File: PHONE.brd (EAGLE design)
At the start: 127 x 53.3 mm, 105 parts, among them IC1 ATMEGA1284P, IC2 ATMEGA16U2-MU, IC3 LTC4054, IC5 LP2985-33DBVR, J1 Power, J2 Analog, J3 Digital_8_13, J4 Digital_0_7, P1 USB-6PSMT, P2 ICSP:MAIN, P3 ICSP:USB, Q1 2N7002 SOT-23, Q2 2N7002, Q3 BC846ALTIG, SW0 0, SW1 1, SW10 *, SW11 #, SW12 LEFT, SW13 DOWN, SW14 RIGHT, SW15 UP, SW2 2, SW3 3, SW4 4, SW5 5, SW6 6, SW7 7, SW8 8, SW9 9, X1 8MHz, X2 16MHz

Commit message: v1.0 release
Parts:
- removed C14: 100nF 0603, freetronics:0603
- removed P3: ICSP:USB, pinhead:2X03
- removed R20, R21: 10K 0603, freetronics:0603
- removed R22: 1K 0603, freetronics:0603
- removed X2: 16MHz, freetronics-master-v1:HC49U-V
- removed Z1, Z2: PGB1010603, freetronics:0603
- added C10: 33pF 0603, freetronics:0603@1
- added C11: 100nF 0603, freetronics:0603
- added JP11: M01PTH, freetronics-original:1X01
- added JP12: MIC, freetronics-master-v1.1:1X02
- added JP13: SPKR, freetronics-master-v1.1:1X02
- added JP14: PIEZO, freetronics-master-v1.1:1X02
- added TP3, TP4, TP5: TEST-POINT, freetronics-original:PAD.02X.02
- C12, C13: value 22pF 0603 -> 47pF 0603; device freetronics:0603 -> freetronics-jon:C0603
- C5: value 47uF 25V -> 100uF 16V
- C6: value 1uF 0603 -> 100uF 16V; device freetronics:0603 -> rcl:PANASONIC_D
- IC2: value ATMEGA16U2-MU -> FT230X; device freetronics-jon:ATMEL_QFN32 -> freetronics-jon:QFN-16
- R11: value 10K 0603 -> 27R 0603
- R12: value 1M 0603 -> 27R 0603
- R13: value 27R 0603 -> 1K 0603
- R14, R15: value 22R 0603 -> 10K 0603
- R16: value 1K 0603 -> 3K3 0603
- R19: value 3K3 0603 -> 1K 0603
- SJ2: value GROUND -> (none); device freetronics-jon:SJC -> freetronics-master-v1.1:SJ
- SJ3: value UBOOT -> (none); device jumper:SJ -> freetronics-master-v1.1:SJ
- moved SJ2 43.3 mm to (27.4, 8.38), turned to 180 degrees
- moved SJ3 35.0 mm to (27.4, 10.7), turned to 180 degrees
- moved R18 33.9 mm to (38.4, 43.4), turned to 180 degrees
- moved R15 28.3 mm to (26.7, 13.0), turned to 0 degrees
- moved C6 27.7 mm to (20.3, 20.1)
- moved R19 21.4 mm to (8.89, 27.2), turned to 180 degrees
- moved R14 19.4 mm to (8.89, 21.1), turned to 180 degrees
- moved R17 17.6 mm to (22.9, 10.4), turned to 270 degrees
- moved R16 16.7 mm to (20.3, 10.4), turned to 270 degrees
- moved U$14 16.5 mm to (63.2, 17.3)
- moved C13 15.0 mm to (9.40, 40.4), turned to 90 degrees
- moved C12 14.1 mm to (9.40, 36.6), turned to 270 degrees
- moved R13 12.6 mm to (8.89, 22.6), turned to 180 degrees
- moved U$5 11.4 mm to (15.4, 44.5)
- moved IC3 10.5 mm to (16.0, 26.9), turned to 0 degrees
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- renumbered IC5 to IC4
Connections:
- removed net MISO2: IC2.17, P3.1
- removed net MOSI2: IC2.16, P3.4
- removed net N$113: C12.2, IC2.2, R12.2, X2.2
- removed net N$114: C13.2, R12.1, R13.2, X2.1
- removed net N$117: C6.1, IC2.27
- removed net RESET2: IC2.24, P3.5, R11.1
- removed net SCK2: IC2.15, P3.3
- removed net UGND: IC2.28, L1.2, P1.GND, SJ2.1
- removed net USBVCC: C1.2, F1.2, IC2.31, IC3.4, R16.1, R17.1
- removed net VIN: J1.8
- new net N$27: JP12.1, SJ2.1
- new net N$28: JP12.2, SJ3.1
- net 5V: now also C1.2, F1.2, IC2.10, IC3.4, R13.1, R14.1; no longer C14.1, IC2.32, IC2.4, P3.2, R11.2
- net D9: now also JP14.1
- net DTR: now also IC2.16; no longer IC2.13, SJ3.2
- net GND: now also C10.1, C11.2, C6.-, IC2.13, IC2.TGND, JP11.1, JP14.2, L1.2, P1.GND, R15.2, R16.2, R17.2, R19.1; no longer C12.1, C13.1, C14.2, C6.2, IC2.EXP, P3.6, R18.2, R19.2, R20.2, R22.1, SJ2.2, SJ3.1
- net N$10: now also R14.2; no longer R17.2
- net N$12: now also R15.1; no longer R18.1
- net N$15: now also R18.1; no longer R21.1
- net N$16: now also C12.1, R12.2; no longer R15.2, Z1.1
- net N$17: now also C13.1, R11.2; no longer R14.2, Z2.1
- net N$18: now also SJ3.2
- net N$19: now also JP13.2
- net N$2: now also C11.1, IC2.8, IC2.9; no longer R13.1
- net N$20: now also JP13.1
- net N$23: now also TP3.P$1
- net N$24: now also TP4.P$1
- net N$25: now also TP5.P$1
- net N$26: now also R18.2; no longer R21.2
- net N$3: now also C12.2, C13.2; no longer Z1.2, Z2.2
- net N$33: now also R16.1; no longer R19.1
- net N$34: now also R17.1; no longer R20.1
- net N$7: now also R19.2; no longer R22.2
- net N$8: now also R13.2; no longer R16.2
- net N$9: now also SJ2.2
- net RD+: now also IC2.6, R12.1; no longer IC2.29, R15.1
- net RD-: now also IC2.7, R11.1; no longer IC2.30, R14.1
- net RXLED: now also IC2.5; no longer IC2.10
- net USBRXD: now also IC2.15; no longer IC2.9
- net USBTXD: now also IC2.2; no longer IC2.8
- net VCC: now also C10.2, C6.+, J1.8
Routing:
- net N$28: track 0.00 -> 99.8 mm, vias 0 -> 3
- net N$27: track 0.00 -> 99.0 mm, vias 0 -> 3
- net USBVCC: track 63.3 -> 0.00 mm, vias 3 -> 0
- net N$19: track 19.3 -> 70.8 mm, vias 0 -> 1
- net N$20: track 12.8 -> 55.5 mm, vias 0 -> 1
- net UGND: track 31.1 -> 0.00 mm, vias 4 -> 0
- net D9: track 33.7 -> 64.2 mm
- net N$18: track 14.2 -> 44.1 mm, vias 0 -> 1
- net N$9: track 21.4 -> 47.6 mm, vias 0 -> 1
- net RESET2: track 24.7 -> 0.00 mm, vias 1 -> 0
- net N$12: track 12.4 -> 32.5 mm
- net VCC: track 104.0 -> 120.6 mm, vias 3 -> 4
- net N$2: track 4.09 -> 19.7 mm, vias 0 -> 2
- net SCK2: track 14.0 -> 0.00 mm
- net N$113: track 13.7 -> 0.00 mm
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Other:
- board text added: "CHRG"
- board text added: "IC2"
- board text added: "MIC"
- board text added: "PIEZO"
- board text added: "SPEAKER"
- board text removed: "ICSP-USB (5V)"
- board text removed: "UBOOT"
- board text removed: "www.freetronics.com"

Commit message: v1.1 release: separated AUDIO_GND from system GND
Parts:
- R10: value 1K5 0603 -> 820R 0603
- R14: value 10K 0603 -> 1K 0603
- R19: value 1K 0603 -> 2K7 0603
- SJ6: device freetronics-jon:SJC -> freetronics-master-v1.1:SJ
- moved U$7 0.25 mm to (30.5, 12.7)
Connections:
- removed net D7: IC1.16, J4.8
- removed net N$28: JP12.2, SJ3.1
- removed net OLED_DNC: JP1.9
- new net AUDIO_GND: JP12.2, S5.42, SJ3.1
- new net D7_OLED_DNC: IC1.16, J4.8, JP1.9
- net GND: no longer S5.42
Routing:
- net AUDIO_GND: track 0.00 -> 118.0 mm, vias 0 -> 4
- net N$28: track 99.8 -> 0.00 mm, vias 3 -> 0
- net D7_OLED_DNC: track 0.00 -> 82.7 mm, vias 0 -> 1
- net D7: track 38.4 -> 0.00 mm
- net GND: track 55.3 -> 48.7 mm
- net N$22: track 46.3 -> 45.6 mm
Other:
- board text added: "v1.1"
- board text removed: "v1.0"

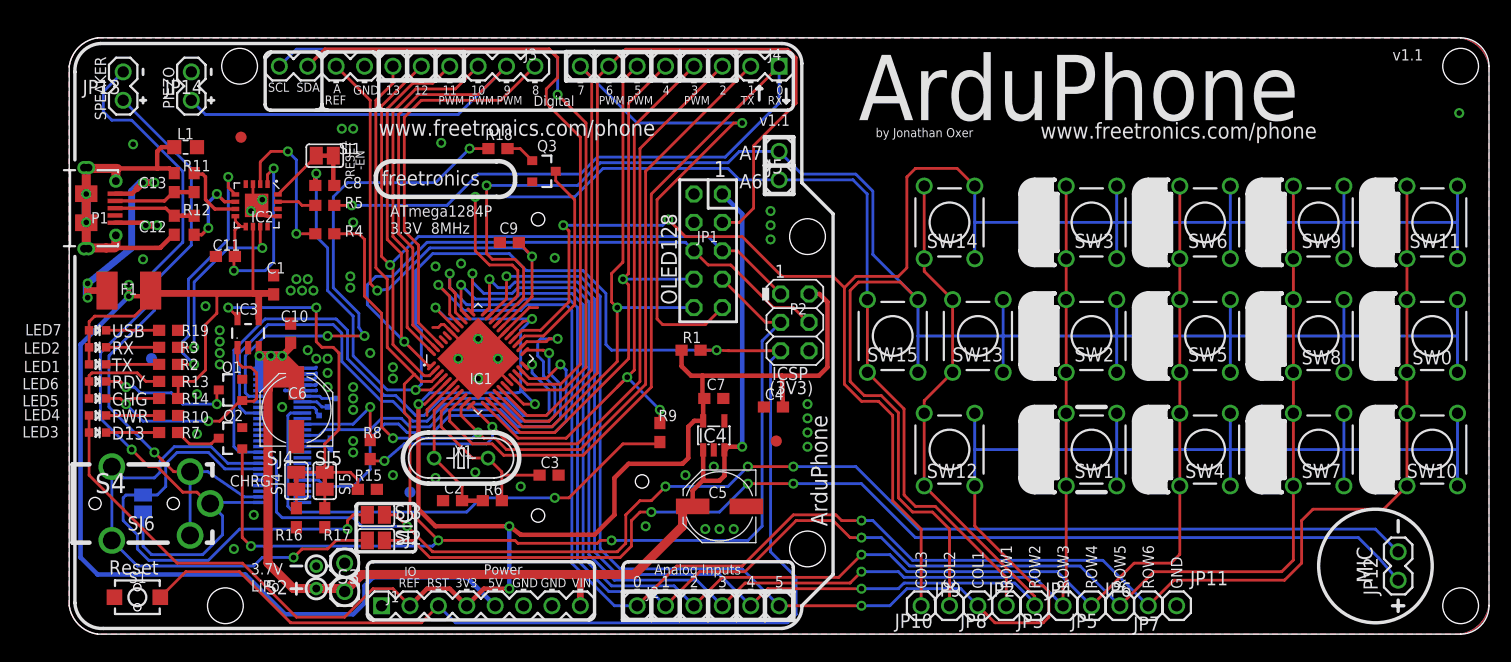
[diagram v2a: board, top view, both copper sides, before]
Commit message: Switched to 4 layers and rerouted for v1.2 release
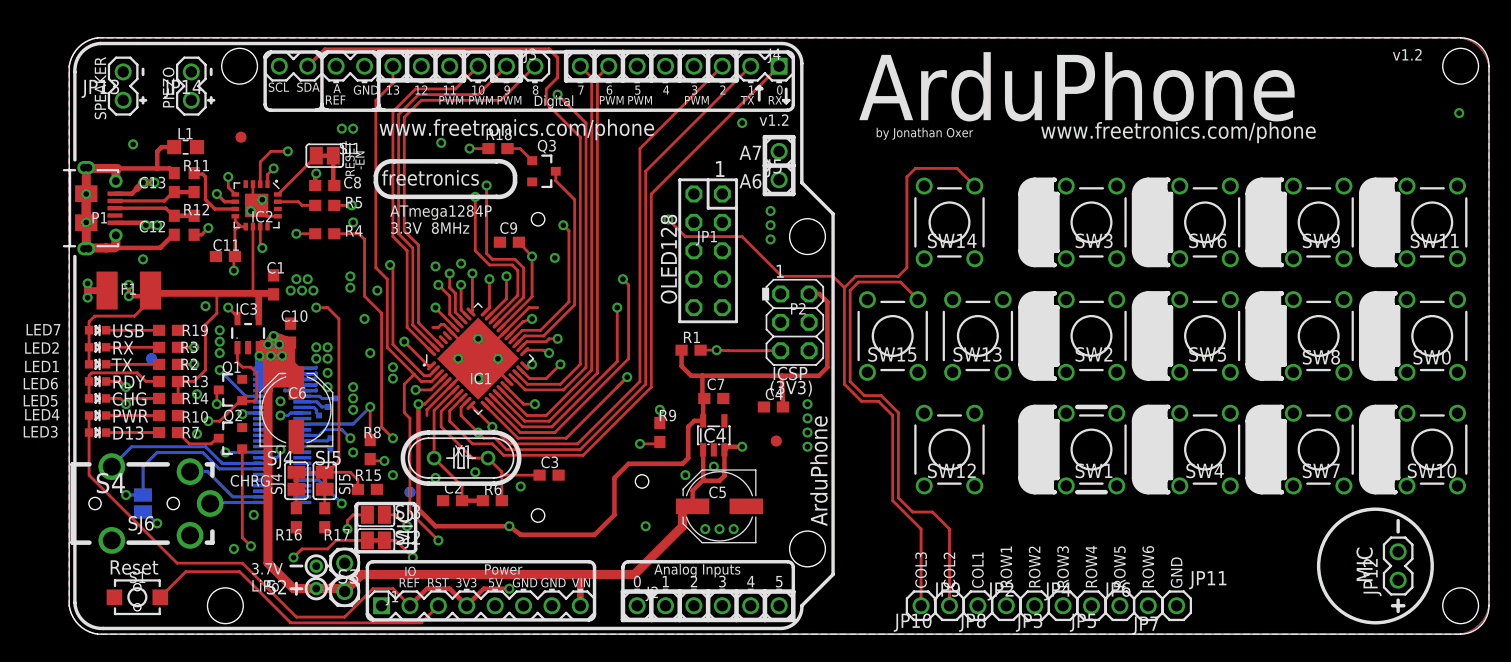
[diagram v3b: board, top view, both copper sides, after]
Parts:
- SJ2: value (none) -> SJCN; device freetronics-master-v1.1:SJ -> freetronics-jon:SJC
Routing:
- net VCC: track 120.6 -> 138.8 mm, vias 4 -> 7
- net ON_KEY: track 52.9 -> 39.2 mm, vias 1 -> 2
- net N$19: track 70.8 -> 62.6 mm
- net N$22: track 45.6 -> 38.4 mm, vias 1 -> 2
- net D13_SCK: track 130.3 -> 123.7 mm, vias 3 -> 2
- net AUDIO_GND: track 118.0 -> 114.7 mm, vias 4 -> 2
- net N$26: track 45.6 -> 47.4 mm
- net GSM_READY: track 39.5 -> 41.0 mm, vias 1 -> 2
- net N$9: track 47.6 -> 46.1 mm
- net N$18: track 44.1 -> 42.8 mm, vias 1 -> 2
- net A2_ROW4: track 131.5 -> 130.2 mm, vias 2 -> 1
- net N$27: track 99.0 -> 98.3 mm, vias 3 -> 1
- net D2_RX1: track 63.7 -> 63.0 mm
- net NET_OK: track 34.2 -> 34.8 mm, vias 1 -> 2
- net DSR0: track 56.1 -> 56.6 mm, vias 1 -> 2
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- added copper zone on layer 15, net GND
- added copper zone on layer 2, net GND
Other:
- board text added: "v1.2"
- board text removed: "v1.1"

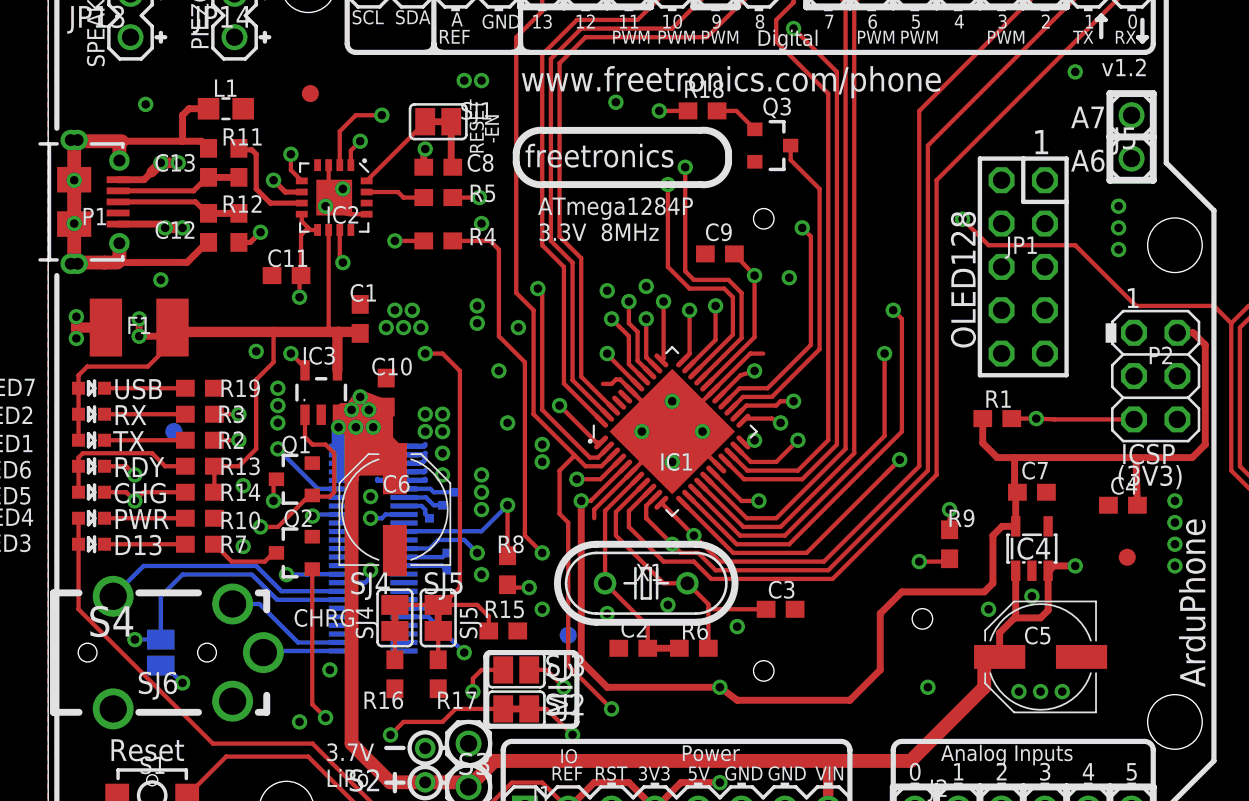
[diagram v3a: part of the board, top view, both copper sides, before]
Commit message: Reconciled schematic and layout using common parts
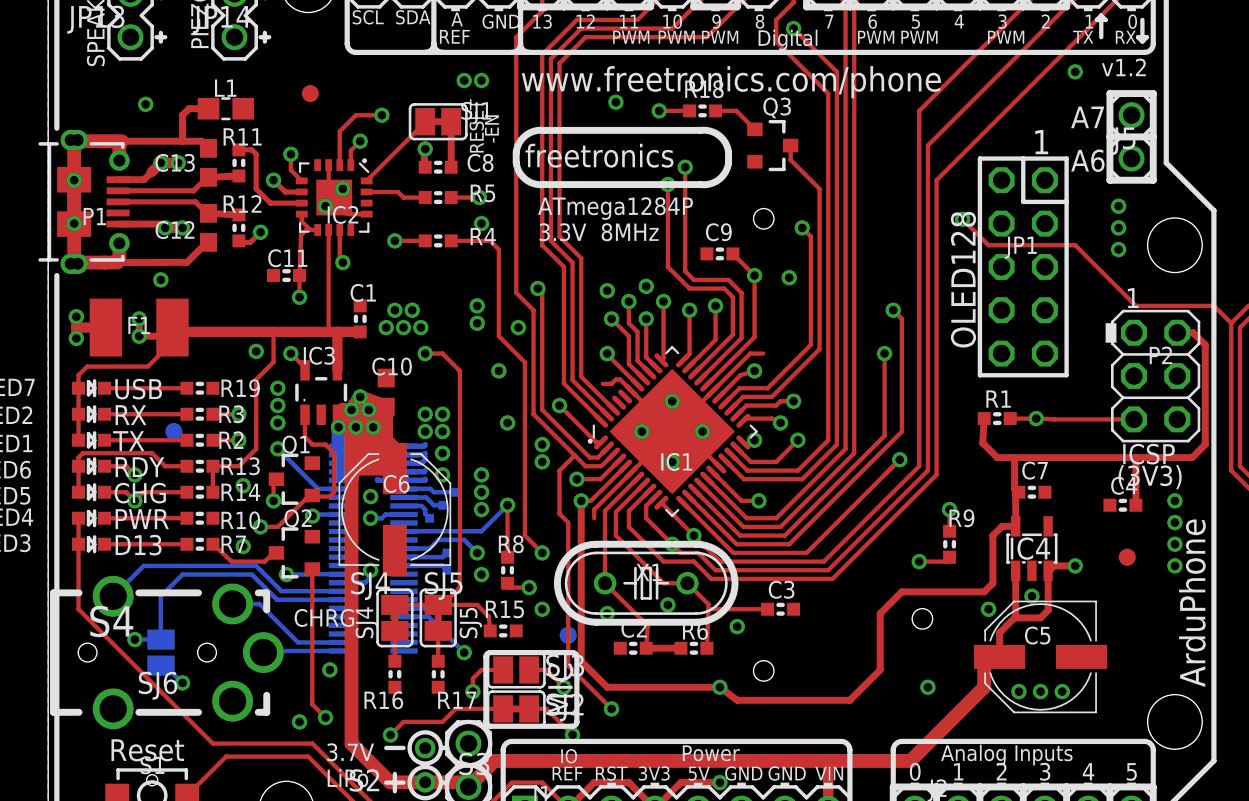
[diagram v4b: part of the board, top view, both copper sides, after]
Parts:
- C1, C11, C2, C3, C4, C7, C8, C9, R1, R10, R11, R12, R13, R14, R15, R16, R17, R18, R19, R2, R3, R4, R5, R6, R7, R8, R9: device freetronics:0603 -> freetronics-master-v1.1:0603
